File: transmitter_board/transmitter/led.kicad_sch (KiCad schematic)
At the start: 4 parts

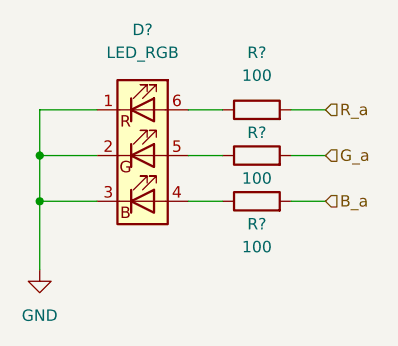
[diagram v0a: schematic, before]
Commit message: finished board schematic
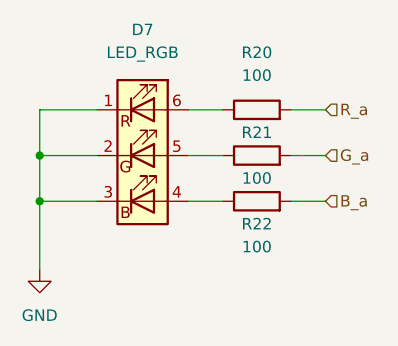
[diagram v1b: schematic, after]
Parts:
- gave numbers to parts that had none: 4
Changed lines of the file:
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@@
   (symbol (lib_id "Device:R") (at 152.4 78.74 90) (unit 1)
     (in_bom yes) (on_board yes) (fields_autoplaced)
-    (property "Reference" "R?" (id 0) (at 152.4 72.39 90))
+    (property "Reference" "R20" (id 0) (at 152.4 72.39 90))
     (property "Value" "100" (id 1) (at 152.4 74.93 90))
     (property "Footprint" "" (id 2) (at 152.4 80.518 90)
@@
   (symbol (lib_id "Device:R") (at 152.4 83.82 90) (unit 1)
     (in_bom yes) (on_board yes)
-    (property "Reference" "R?" (id 0) (at 152.4 81.28 90))
+    (property "Reference" "R21" (id 0) (at 152.4 81.28 90))
     (property "Value" "100" (id 1) (at 152.4 86.36 90))
     (property "Footprint" "" (id 2) (at 152.4 85.598 90)
@@
   (symbol (lib_id "Device:R") (at 152.4 88.9 90) (unit 1)
     (in_bom yes) (on_board yes)
-    (property "Reference" "R?" (id 0) (at 152.4 91.44 90))
+    (property "Reference" "R22" (id 0) (at 152.4 91.44 90))
     (property "Value" "100" (id 1) (at 152.4 93.98 90))
     (property "Footprint" "" (id 2) (at 152.4 90.678 90)
@@
   (symbol (lib_id "power:GND") (at 128.27 96.52 0) (unit 1)
     (in_bom yes) (on_board yes) (fields_autoplaced)
-    (property "Reference" "#PWR?" (id 0) (at 128.27 102.87 0)
+    (property "Reference" "#PWR0142" (id 0) (at 128.27 102.87 0)
       (effects (font (size 1.27 1.27)) hide)
     )
@@
   (symbol (lib_id "Device:LED_RGB") (at 139.7 83.82 0) (unit 1)
     (in_bom yes) (on_board yes) (fields_autoplaced)
-    (property "Reference" "D?" (id 0) (at 139.7 69.85 0))
+    (property "Reference" "D7" (id 0) (at 139.7 69.85 0))
     (property "Value" "LED_RGB" (id 1) (at 139.7 72.39 0))
     (property "Footprint" "LED_SMD:LED_RGB_5050-6" (id 2) (at 139.7 85.09 0)
